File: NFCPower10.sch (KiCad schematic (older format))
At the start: 33 parts

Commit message: add si5351. and separate power side logic SCLP SDAP and IRQP when power not applied to +5VP.
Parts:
- added C10, C9: CC0603KPX7R9BB104, project:YAGEO-CC0603-0-0-0, symbol project:CC0603KPX7R9BB104
- added Q1, Q2, Q3: BSS138, ON_Semiconductor-318-08-01_2018-AS-*, symbol project:BSS138
- added R10, R11, R12, R124, R125, R13: RC0603FR-0710KL, Yageo-RC0603-0-0-*, symbol project:RC0603FR-0710KL
- added U3: Si5351A-B-GM, Silicon_Labs-Si5351A-B-GM-*, symbol project:Si5351A-B-GM
- added Y2: ABM8G-25.000MHz-B4Y-T, Abracon-ABM8G-25.000MHz-B4Y-T-*, symbol project:ABM8G-25.000MHz-B4Y-T
- gave numbers to parts that had none: 33
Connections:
- net labels added: IRQP, OEB, RED, SCLP, SDAP, SSEN
- wire segments 210 -> 264
- no-connect marks 30 -> 31
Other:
- note added: "Button Interrupt Request"
- note added: "Button Reset"
- note added: "In Circuit Serial Programing"
- note removed: "In Circuit\nSerial\nPrograming"
- note removed: "Push Button Interrupt Request"
- note removed: "Push Button Reset"
- moved on the sheet: D3, D4, D5, DS1, J3, R1, R2, R7, R8, R9, SW1, SW2

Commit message: update
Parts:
- added Q5, Q?: BSS138, ON_Semiconductor-318-08-01_2018-AS-*, symbol project:BSS138
- added R17, R18, R19: RC0603FR-0710KL, Yageo-RC0603-0-0-*, symbol project:RC0603FR-0710KL
- renumbered C4 to C3, C3 to C4, DS1 to D3, D3 to D4, D4 to D6, J5 to J4, J4 to J5, R124 to R10, R10 to R11, R11 to R12, R125 to R13, R12 to R14, R13 to R15, R7 to R2, R2 to R3, R3 to R4, R4 to R5, R5 to R6, R6 to R7
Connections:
- net labels added: RXP, TXP
- wire segments 264 -> 304
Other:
- moved on the sheet: C1, C2, C3, C6, C8, C9, D3, D4, D5, D6, J2, J3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

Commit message: update
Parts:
- C4, C5: footprint YAGEO-CC0805-0-0-* -> project:YAGEO-CC0805-0-0-0
- C6, C8: footprint TDK-CGA3E-0.3-0.1-0-0-* -> project:TDK-CGA3E-0.3-0.1-0-0-IPC_A
- D1, D2: footprint On_Semiconductor-BAT54T1G-* -> project:On_Semiconductor-BAT54T1G-Manufacturer_Recommended
- D3: footprint Vishay_Lite-On-LTST-C190TBKT-* -> project:Vishay_Lite-On-LTST-C190TBKT-Manufacturer_Recommended
- D4: footprint Lite-On-LTST-C190KRKT-* -> project:Lite-On-LTST-C190KRKT-MFG
- D5: footprint Lite-On-LTST-C190KGKT-* -> project:Lite-On-LTST-C190KGKT-MFG
- D6: footprint Lite-On-LTST-C190KSKT-* -> project:Lite-On-LTST-C190KSKT-MFG
- J1: footprint CUI-PJ-002AH-0-0-* -> project:CUI_PJ-002AH
- J2: footprint Molex-475890001-* -> project:Molex-475890001-MFG
- J3: footprint (none) -> Pin_Headers:Pin_Header_Straight_2x03_Pitch2.54mm
- J5: footprint Samtec-SSW-106-02-T-S-* -> project:Samtec-SSW-106-02-T-S-Manufacturer_Recommended
- Q1, Q2, Q3, Q5: footprint ON_Semiconductor-318-08-01_2018-AS-* -> project:ON_Semiconductor-318-08-01_2018-AS-MFG
- Q4: renamed from Q?; footprint ON_Semiconductor-318-08-01_2018-AS-* -> project:ON_Semiconductor-318-08-01_2018-AS-MFG
- R1, R10, R11, R12, R13, R14, R15, R17, R18, R19, R2, R3, R4, R5, R6, R7, R8, R9: footprint Yageo-RC0603-0-0-* -> project:Yageo-RC0603-0-0-IPC_A
- SW1, SW2: footprint TE_Connectivity-FSM2JSMAA-* -> project:TE_Connectivity-FSM2JSMAA-MFG
- U1: footprint Microchip___Atmel-ATMEGA328P-MU-* -> project:Microchip___Atmel-ATMEGA328P-MU-Level_A
- U2: footprint FTDI-QFN-20-0-0-* -> project:FTDI-QFN-20-0-0-MFG
- U3: footprint Silicon_Labs-Si5351A-B-GM-* -> project:Silicon_Labs-Si5351A-B-GM-Level_A
- Y1: footprint Epson-TSX-3225_16.0000MF09Z-AC3-* -> project:Epson-TSX-3225_16.0000MF09Z-AC3-0
- Y2: footprint Abracon-ABM8G-25.000MHz-B4Y-T-* -> project:Abracon-ABM8G-25.000MHz-B4Y-T-0

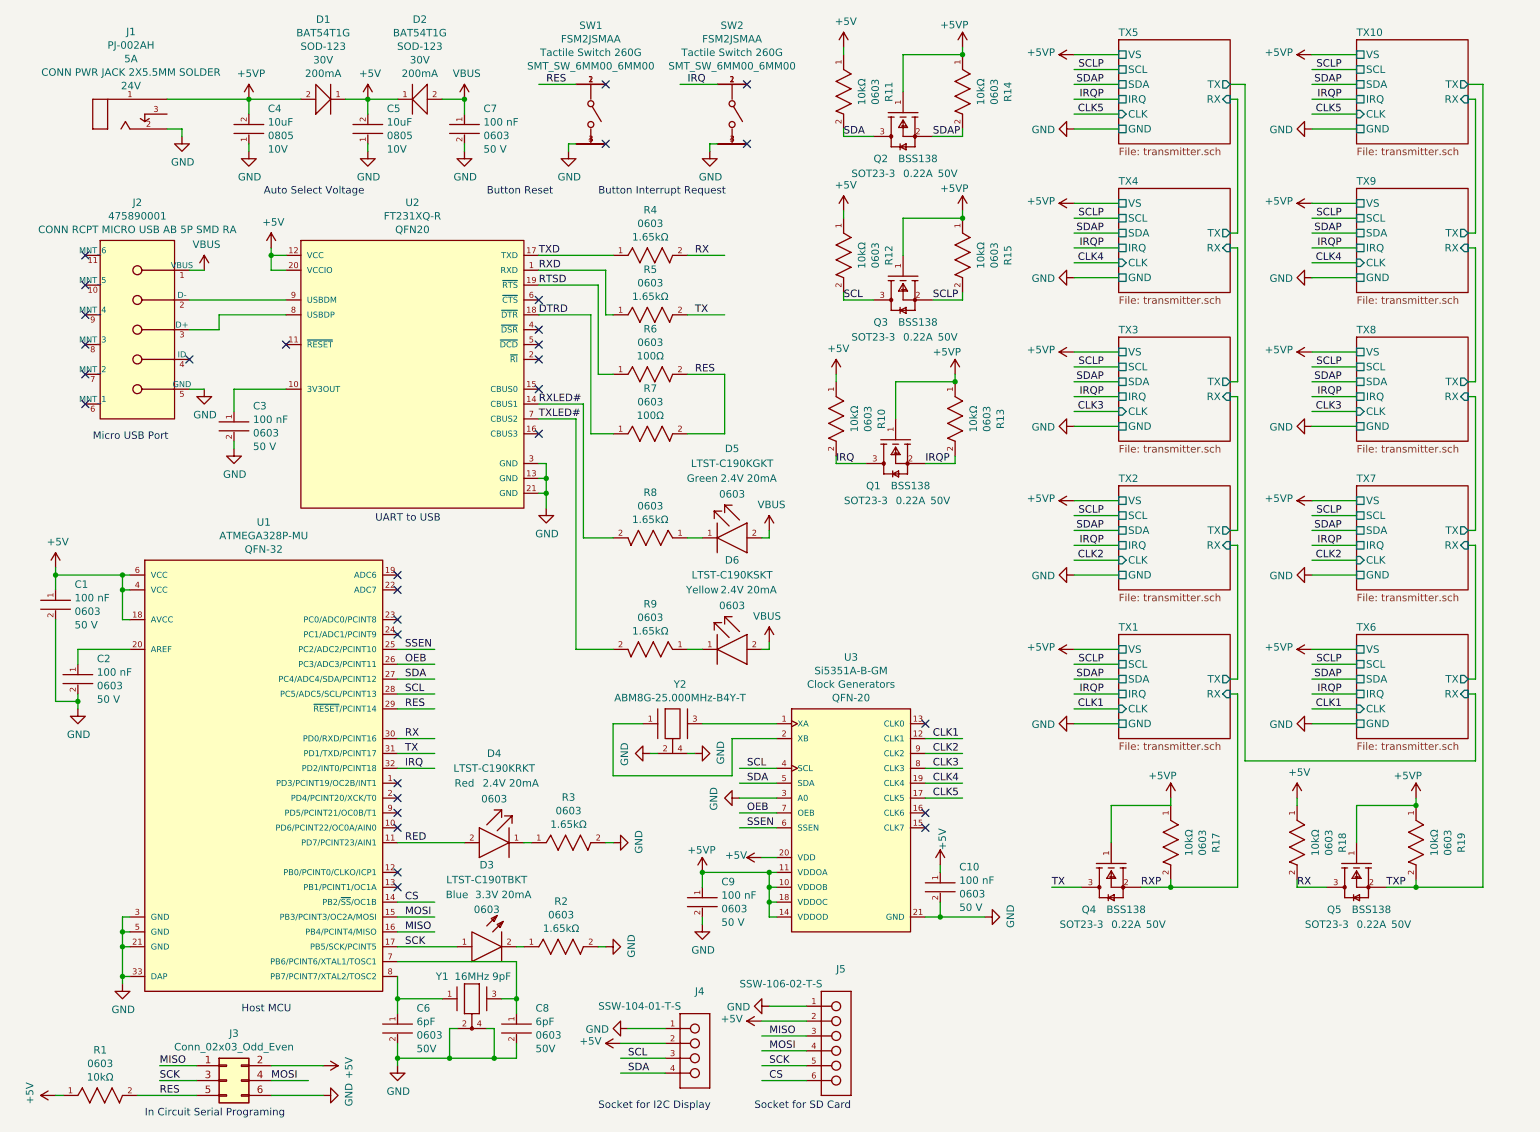
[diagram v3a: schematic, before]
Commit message: continue routing. add INA219 to monitor +5VP rail.
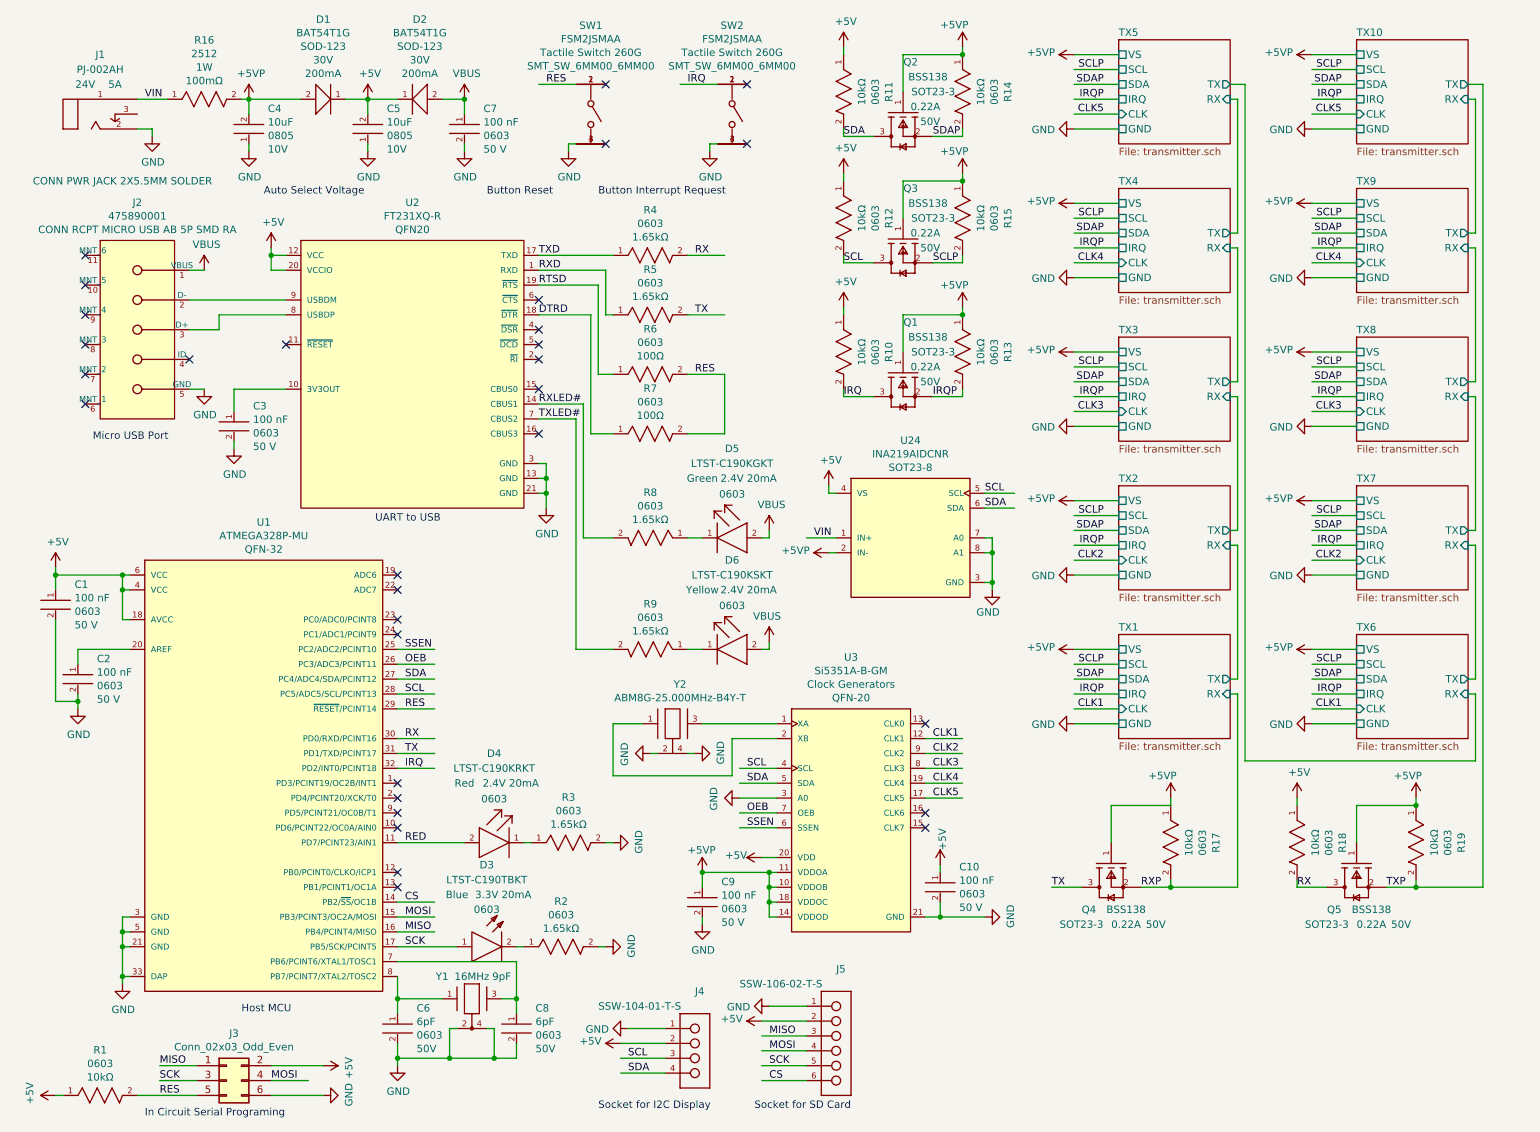
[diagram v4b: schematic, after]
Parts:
- added R16: RL2512FK-070R1L, project:YAGEO-RL2512-02_2018-10-MFG, symbol project:RL2512FK-070R1L
- added U24: INA219AIDCNR, project:Texas_Instruments-DCN0008A-0-0-MFG, symbol project:INA219AIDCNR
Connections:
- net labels added: VIN
- wire segments 304 -> 317
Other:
- moved on the sheet: J1, Q1, R10, R12, R13, R15

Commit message: rev 2
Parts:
- removed C10, C9: CC0603KPX7R9BB104, project:YAGEO-CC0603-0-0-0, symbol project:CC0603KPX7R9BB104
- removed R11, R12: RC0603FR-0710KL, project:Yageo-RC0603-0-0-IPC_A, symbol project:RC0603FR-0710KL
- removed R6, R7: RC0603FR-07100RL, project:Yageo-RC0603-0-0-IPC_A, symbol project:RC0603FR-07100RL
- removed U3: Si5351A-B-GM, project:Silicon_Labs-Si5351A-B-GM-Level_A, symbol project:Si5351A-B-GM
- removed Y2: ABM8G-25.000MHz-B4Y-T, project:Abracon-ABM8G-25.000MHz-B4Y-T-0, symbol project:ABM8G-25.000MHz-B4Y-T
- added C39: CC0603KPX7R9BB104, project:YAGEO-CC0603-0-0-0, symbol project:CC0603KPX7R9BB104
- added FID1, FID2, FID3: fiducial, Fiducials:Fiducial_1mm_Dia_2.54mm_Outer_CopperTop, symbol project:fiducial
- added J9: SSW-104-01-T-S, project:Samtec-SSW-104-01-T-S-Manufacturer_Recommended, symbol project:SSW-104-01-T-S
- added MT1, MT2, MT3, MT4: Mount Hole M3, Mounting_Holes:MountingHole_3.2mm_M3, symbol Connector_Generic:Conn_01x01
- added R11, R12: RC0603FR-071K65L, project:Yageo-RC0603-0-0-IPC_A, symbol project:RC0603FR-071K65L
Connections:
- net labels added: CSS, ENCA, ENCB, ENED1, ENED2, GRN, IED, RXT, SDCS, TXT
- net labels removed: CS, OEB, RTSD, SSEN
- wire segments 317 -> 382
- no-connect marks 31 -> 27
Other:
- note added: "5VP Rail Voltage and Current Sensor"
- note added: "I2C and SPI Devices \nOperating at 3.3V and 2.8V"
- note added: "Socket for Encoder"
- moved on the sheet: D5, D6, J4, J5, Q4, Q5, R17, R18, R19, R4, R5, R8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
